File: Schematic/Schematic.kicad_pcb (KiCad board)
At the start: 2 copper layers, 76 parts, among them J1 Conn_02x08_Odd_Even, J2 Conn_01x08, J3 Conn_01x04_Pin, J4 Conn_02x01, J5 Conn_02x05_Odd_Even, J6 Conn_01x03_Pin, J7 Conn_01x02_Pin, SW1 SW_Push, U1 74LS08, U2 STM32F091RCT6, U3 LM386, U4 LM2678S-12, U5 LD1117S33TR_SOT223

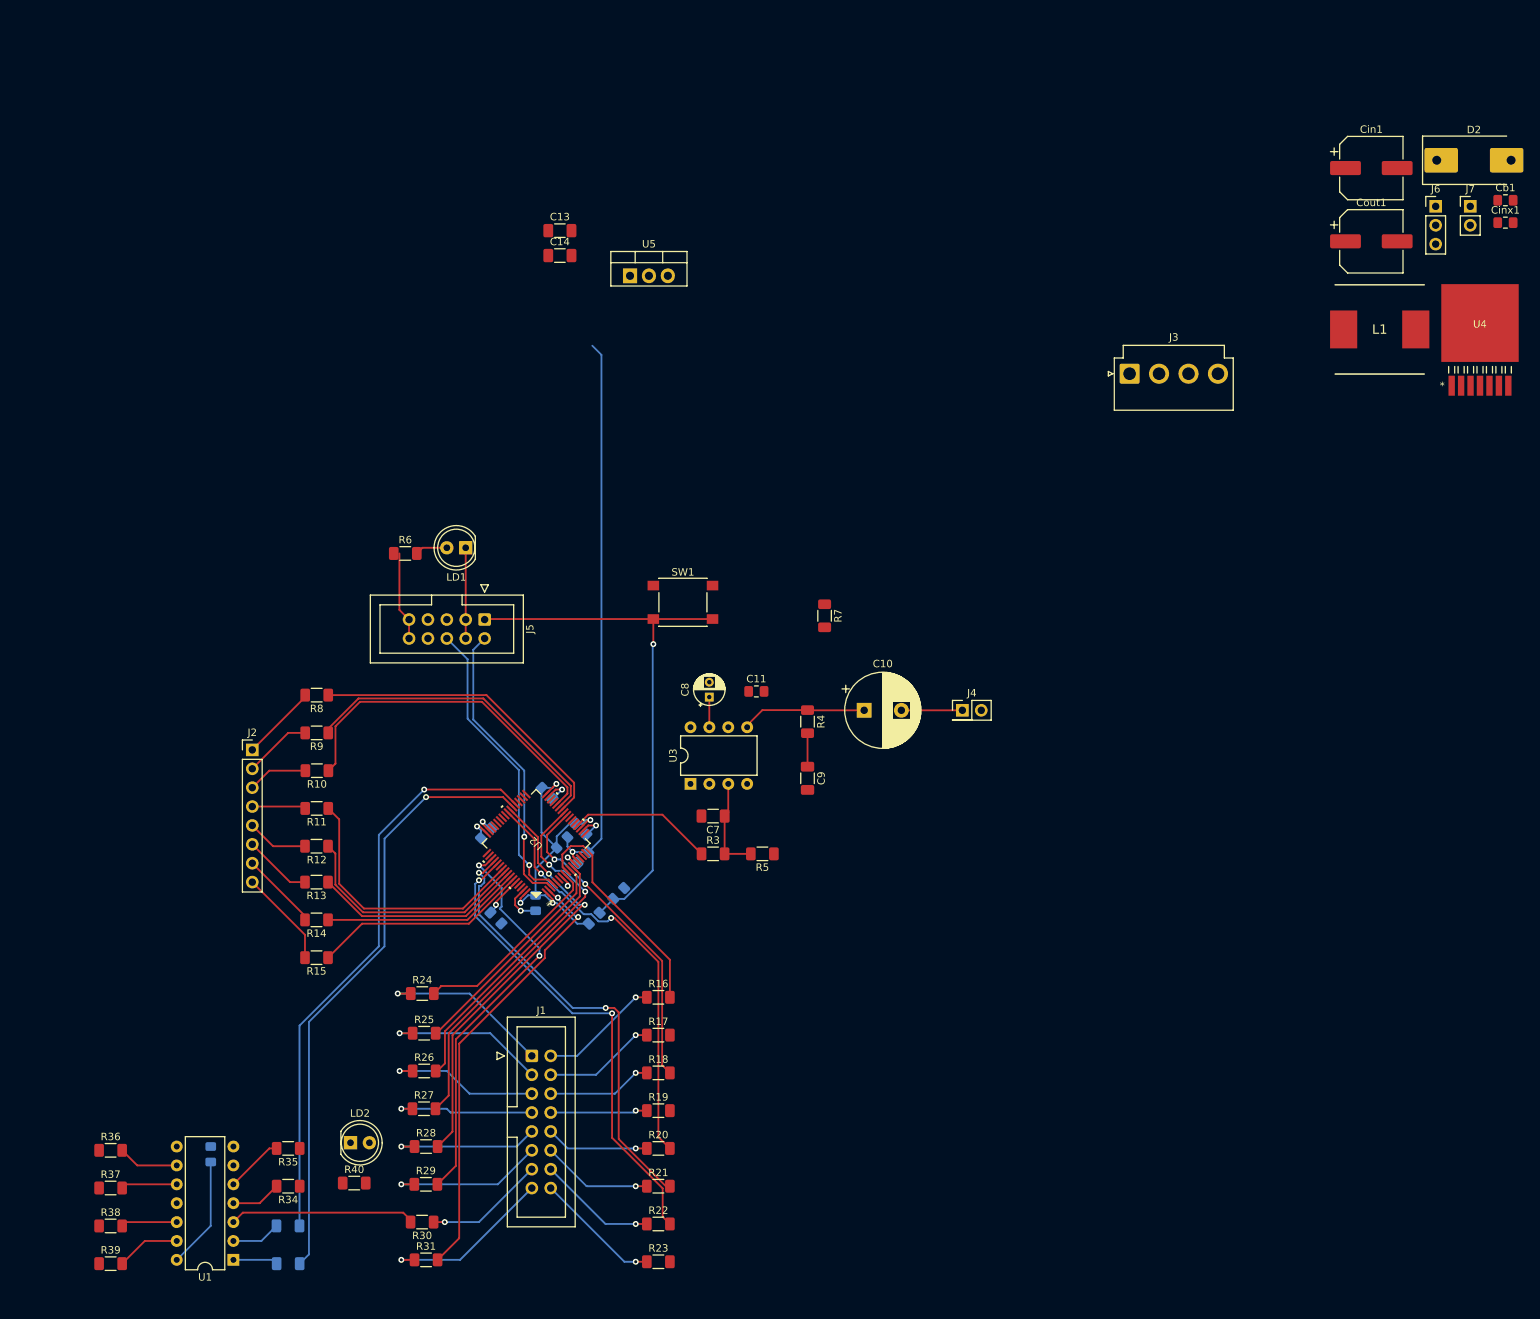
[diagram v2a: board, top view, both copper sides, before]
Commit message: Most of the schematic and PCB layout.
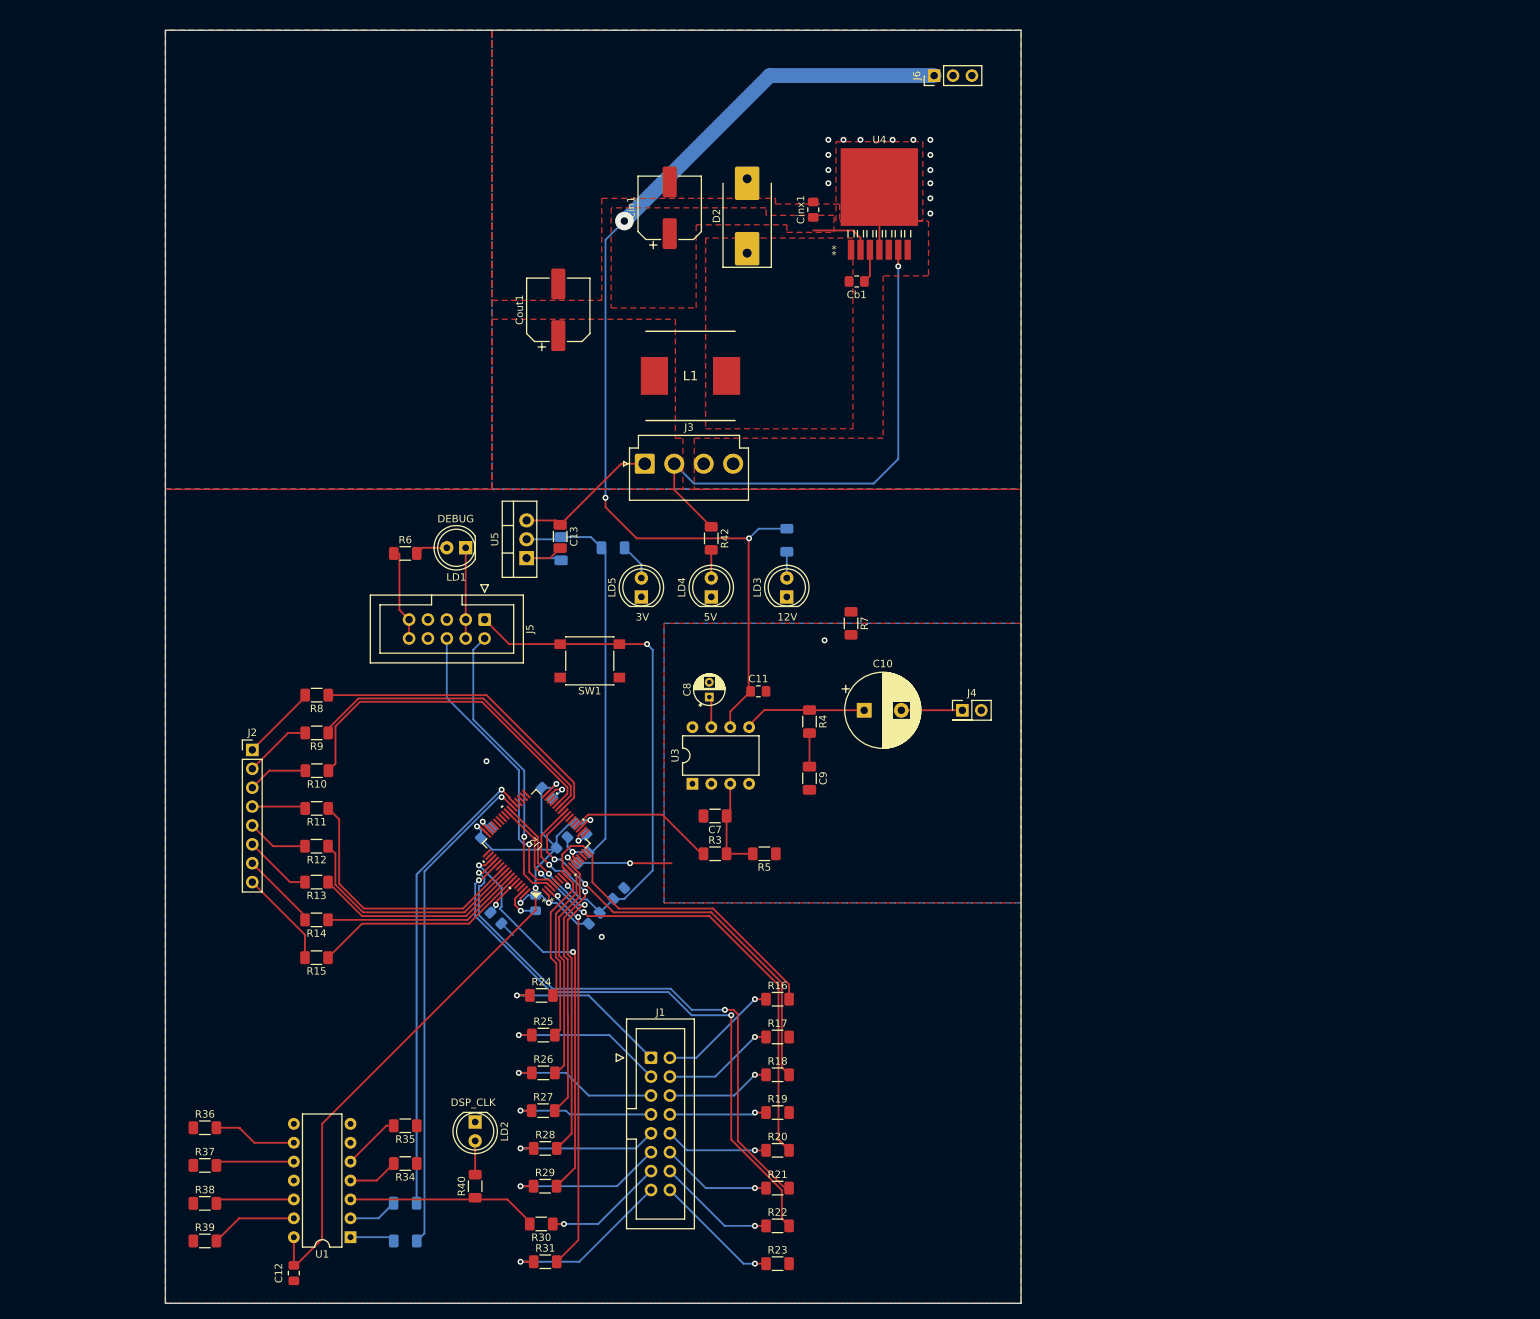
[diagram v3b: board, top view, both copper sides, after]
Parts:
- removed J7: Conn_01x02_Pin, Connector_PinHeader_2.54mm:PinHeader_1x02_P2.54mm_Vertical
- added LD3: LED_Blue, LED_THT:LED_D5.0mm, F.Cu at (139.7, 100.6)
- added LD4: LED_Green, LED_THT:LED_D5.0mm, F.Cu at (129.5, 100.6)
- added LD5: LED_Red, LED_THT:LED_D5.0mm, F.Cu at (120.1, 100.6)
- added R41: 56k, Resistor_SMD:R_1206_3216Metric_Pad1.30x1.75mm_HandSolder, B.Cu at (139.7, 93.0)
- added R42: 5.6k, Resistor_SMD:R_1206_3216Metric_Pad1.30x1.75mm_HandSolder, F.Cu at (129.5, 92.7)
- added R43: 5.6k, Resistor_SMD:R_1206_3216Metric_Pad1.30x1.75mm_HandSolder, B.Cu at (116.3, 94.0)
- C12: moved to F.Cu
- C14: moved to B.Cu
- R40: value 5.1k -> 5.6k
- R6: value 5.1k -> 10k
- moved Cout1 109.7 mm to (109.0, 62.0), turned to 90 degrees
- moved D2 98.0 mm to (134.4, 49.4), turned to 90 degrees
- moved Cin1 94.5 mm to (124.0, 48.3), turned to 90 degrees
- moved Cinx1 93.1 mm to (143.3, 48.5), turned to 90 degrees
- moved L1 92.9 mm to (126.7, 70.9), turned to 180 degrees
- moved Cb1 87.9 mm to (149.1, 58.2), turned to 180 degrees
- moved U4 82.8 mm to (152.1, 45.6)
- moved J6 69.7 mm to (159.5, 30.5), turned to 90 degrees
- moved J3 66.3 mm to (120.6, 82.7)
- moved C13 41.1 mm to (109.2, 92.5), turned to -90 degrees
- moved U5 40.4 mm to (104.7, 95.4), turned to 90 degrees
- moved C14 39.4 mm to (109.3, 94.1), turned to -90 degrees
- moved C12 19.5 mm to (73.4, 191.5), turned to -90 degrees
- moved LD2 17.0 mm to (97.8, 171.2), turned to -90 degrees
- moved R40 16.3 mm to (97.8, 179.8), turned to 90 degrees
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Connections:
- net Net-(D2-K) renamed /power/VSW
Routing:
- net +12V: track 0.00 -> 150.8 mm, vias 0 -> 3
- net +5V: track 0.00 -> 90.8 mm, vias 0 -> 1
- net +3V0: track 62.8 -> 126.9 mm, vias 5 -> 6
- net GND: track 28.9 -> 48.4 mm, vias 4 -> 20
- net PC9: track 57.0 -> 73.2 mm
- net VA: track 75.2 -> 59.1 mm
- net PC12: track 63.8 -> 80.0 mm
- net PC11: track 60.1 -> 76.1 mm
- net PC6: track 78.8 -> 63.2 mm
- net PC7: track 82.1 -> 66.8 mm
- net PC4: track 43.1 -> 57.7 mm
- net PC1: track 31.0 -> 45.3 mm
- net GNDA: track 2.93 -> 15.6 mm, vias 1 -> 3
- net PC0: track 27.1 -> 18.5 mm
- net PC3: track 37.0 -> 30.3 mm
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- added copper zone on F.Cu, net +12V
- added copper zone on F.Cu, net +5V
- added copper zone on F.Cu, net /power/VSW
- added copper zone on B.Cu, net GND
- added copper zone on F.Cu, net GND
- added copper zone on B.Cu, net GNDA
- added copper zone on F.Cu, net GNDA
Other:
- board outline added: 115.1 x 171.2 mm
- board text added: "12V"
- board text added: "3V"
- board text added: "5V"
- board text added: "DEBUG"
- board text added: "DSP_CLK"

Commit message: Added stuff from today
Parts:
- added H1: MountingHole, MountingHole:MountingHole_5mm, F.Cu at (63.0, 30.5)
- added H2: MountingHole, MountingHole:MountingHole_5mm, F.Cu at (62.2, 189.7)
- added H3: MountingHole, MountingHole:MountingHole_5mm, F.Cu at (164.3, 188.7)
- added H4: MountingHole, MountingHole:MountingHole_5mm, F.Cu at (165.4, 29.7)
- added J10: Conn_01x03_Pin, Connector_PinSocket_2.54mm:PinSocket_1x03_P2.54mm_Vertical, F.Cu at (78.0, 47.8)
- added J11: Conn_01x03_Pin, Connector_PinSocket_2.54mm:PinSocket_1x03_P2.54mm_Vertical, F.Cu at (82.1, 47.8)
- added J12: Conn_01x03_Pin, Connector_PinSocket_2.54mm:PinSocket_1x03_P2.54mm_Vertical, F.Cu at (66.0, 63.2)
- added J13: Conn_01x03_Pin, Connector_PinSocket_2.54mm:PinSocket_1x03_P2.54mm_Vertical, F.Cu at (70.2, 63.2)
- added J14: Conn_01x03_Pin, Connector_PinSocket_2.54mm:PinSocket_1x03_P2.54mm_Vertical, F.Cu at (74.3, 63.2)
- added J15: Conn_01x03_Pin, Connector_PinSocket_2.54mm:PinSocket_1x03_P2.54mm_Vertical, F.Cu at (78.5, 63.2)
- added J16: Conn_01x03_Pin, Connector_PinSocket_2.54mm:PinSocket_1x03_P2.54mm_Vertical, F.Cu at (82.6, 63.2)
- added J17: Conn_01x03_Pin, Connector_PinSocket_2.54mm:PinSocket_1x03_P2.54mm_Vertical, F.Cu at (144.5, 150.6)
- added J7: Conn_01x03_Pin, Connector_PinSocket_2.54mm:PinSocket_1x03_P2.54mm_Vertical, F.Cu at (65.5, 47.8)
- added J8: Conn_01x03_Pin, Connector_PinSocket_2.54mm:PinSocket_1x03_P2.54mm_Vertical, F.Cu at (69.7, 47.8)
- added J9: Conn_01x03_Pin, Connector_PinSocket_2.54mm:PinSocket_1x03_P2.54mm_Vertical, F.Cu at (73.8, 47.8)
- added LD6: LED_Red, LED_THT:LED_D5.0mm, F.Cu at (64.3, 107.2)
- added R44: 5.6k, Resistor_SMD:R_1206_3216Metric_Pad1.30x1.75mm_HandSolder, F.Cu at (71.9, 107.4)
- added R45: 1k, Resistor_SMD:R_1206_3216Metric_Pad1.30x1.75mm_HandSolder, F.Cu at (65.5, 174.3)
- added R46: 1k, Resistor_SMD:R_1206_3216Metric_Pad1.30x1.75mm_HandSolder, F.Cu at (65.5, 177.5)
- added REF**: PrototypeBoard, Custom:PrototypeBoard, F.Cu at (144.5, 154.7)
- added U6: MAX7375AXR805, Package_TO_SOT_SMD:SOT-323_SC-70, F.Cu at (107.7, 143.5)
- J6: footprint Connector_PinHeader_2.54mm:PinHeader_1x03_P2.54mm_Vertical -> Connector_PinSocket_2.54mm:PinSocket_1x03_P2.54mm_Vertical
- moved R34 31.9 mm to (65.5, 154.5), turned to 0 degrees
- moved R35 26.8 mm to (65.5, 157.8), turned to 0 degrees
- moved R39 16.7 mm to (65.5, 171.0)
- moved R38 15.0 mm to (65.5, 167.7)
- moved R37 13.3 mm to (65.5, 164.4)
- moved R36 11.6 mm to (65.5, 161.1)
- moved J6 7.95 mm to (162.6, 37.8)
- moved C1 0.25 mm to (117.3, 140.5)
- moved R1 0.25 mm to (114.1, 143.8)
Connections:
- R38 pad 1: GND -> unconnected-(R38-Pad1)
- R38 pad 2: Net-(R38-Pad2) -> Net-(R35-Pad2)
- R39 pad 1: GND -> unconnected-(R39-Pad1)
- R39 pad 2: Net-(R39-Pad2) -> Net-(R34-Pad2)
- U1 pad 10: Net-(R37-Pad2) -> Net-(U1-Pad10)
- U1 pad 11: unconnected-(U1-Pad11) -> Net-(U1-Pad10)
- U1 pad 12: Net-(R38-Pad2) -> Net-(R36-Pad2)
- U1 pad 13: Net-(R39-Pad2) -> Net-(R37-Pad2)
- U1 pad 6: unconnected-(U1-Pad6) -> Net-(U1-Pad6)
- U1 pad 8: unconnected-(U1-Pad8) -> PB15
- U1 pad 9: Net-(R36-Pad2) -> Net-(U1-Pad6)
- U2 pad 14: unconnected-(U2-PA0-Pad14) -> PA0
- U2 pad 15: unconnected-(U2-PA1-Pad15) -> PA1
- U2 pad 16: unconnected-(U2-PA2-Pad16) -> PA2
- U2 pad 17: unconnected-(U2-PA3-Pad17) -> PA3
- U2 pad 21: unconnected-(U2-PA5-Pad21) -> Net-(U2-PA5)
- U2 pad 3: /microprocessor/SWDIO_IN -> Net-(U2-PC14-OSC32_IN)
- U2 pad 4: /microprocessor/SWCLK_IN -> unconnected-(U2-PC15-OSC32_OUT-Pad4)
- U2 pad 45: unconnected-(U2-PA12-Pad45) -> /microprocessor/SWCLK_IN
- U2 pad 46: unconnected-(U2-PA13-Pad46) -> /microprocessor/SWDIO_IN
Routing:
- net PA2: track 0.00 -> 44.0 mm, vias 0 -> 2
- net PA1: track 0.00 -> 41.9 mm, vias 0 -> 2
- net PA0: track 0.00 -> 41.0 mm, vias 0 -> 2
- net /microprocessor/SWCLK_IN: track 40.4 -> 27.8 mm
- net Net-(R39-Pad2): track 11.7 -> 0.00 mm
- net Net-(R36-Pad2): track 11.4 -> 0.00 mm
- net Net-(R38-Pad2): track 10.6 -> 0.00 mm
- net Net-(R37-Pad2): track 10.6 -> 0.00 mm
- net +3V0: track 126.9 -> 136.1 mm
- net /microprocessor/SWDIO_IN: track 39.6 -> 31.3 mm
- net Net-(R35-Pad2): track 7.81 -> 0.00 mm
- net Net-(U1-Pad6): track 0.00 -> 7.62 mm
- net Net-(R34-Pad2): track 6.76 -> 0.00 mm
- net Net-(U2-PC14-OSC32_IN): track 0.00 -> 4.34 mm
- net PC13: track 53.3 -> 57.3 mm
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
